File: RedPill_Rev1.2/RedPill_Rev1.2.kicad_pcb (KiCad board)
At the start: 2 copper layers, 21.6 x 66 mm, 26 parts, among them J1 Conn_01x04, J2 Conn_01x04, J3 USB_B_Mini, J5 Pin_01x20, J6 Pin_01x20, SW1 SW_Push, U1 TLV1117-33, U2 STM32G0B1KET6, X1 SG-5032CAN

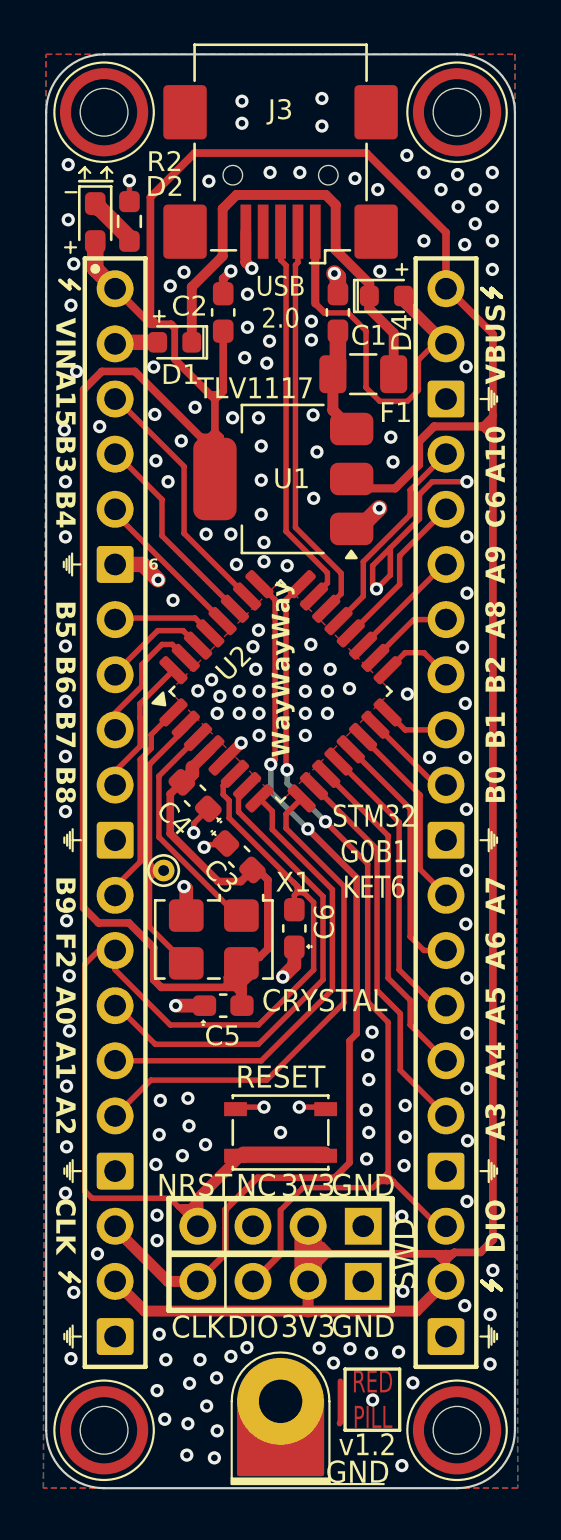
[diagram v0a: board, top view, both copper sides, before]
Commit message: Made silkscreen pretty
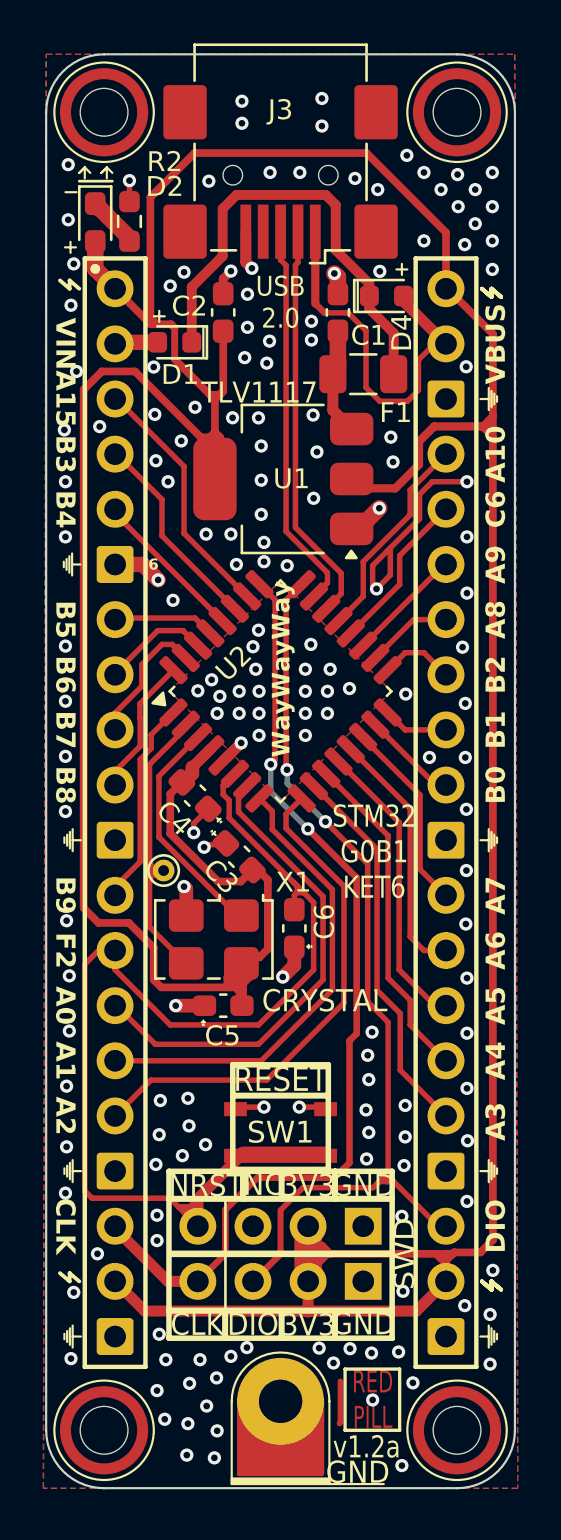
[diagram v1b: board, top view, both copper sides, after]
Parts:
- F1: value Polyfuse_Small -> Polyfuse
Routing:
- net GND: vias 177 -> 176
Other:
- board text added: "v1.2a"
- board text removed: "v1.2"

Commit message: v1.2a
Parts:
- H1: value MountingHole -> M2_2.2mm_TL
- H2: value MountingHole -> M2_2.2mm_TR
- H3: value MountingHole -> M2_2.2mm_BL
- H4: value MountingHole -> M2_2.2mm_BR
- J1, J2: value Conn_01x04 -> Pin_01x04
- SW1: value SW_Push -> PTS810
- TP5: value TestPoint -> GND Test
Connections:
- net /REG_IN renamed /DIODE_VOUT
- net /SYS_SWCLK renamed /SWCLK
- net /SYS_SWDIO renamed /SWDIO
- J3 pad 6: unconnected-(J3-Shield-Pad6)_1 -> /SHIELD
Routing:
- net GND: track 31.2 -> 29.2 mm, vias 176 -> 181
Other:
- board text added: "BLKPILL"
- board text removed: "RED PILL"
